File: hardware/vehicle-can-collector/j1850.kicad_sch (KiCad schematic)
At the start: 28 parts, among them Q801 2N7002, Q802 2N7002, Q803 2N7002, Q804 2N7002, Q805 2N7002, Q806 DMG2301L, Q807 2N7002, U801 AS2333Q

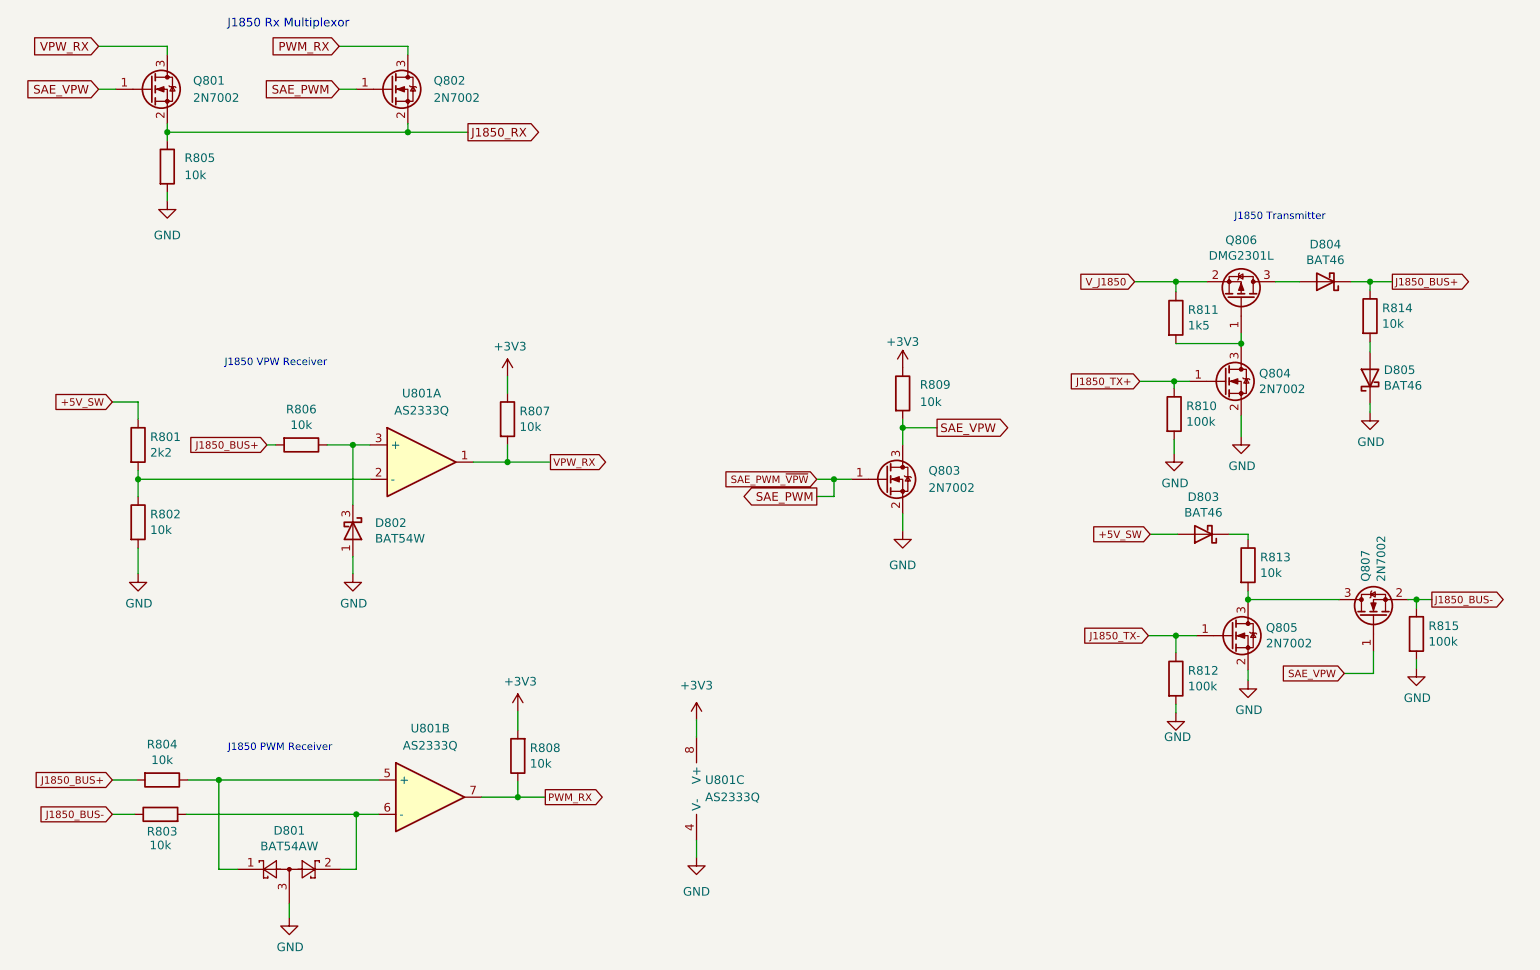
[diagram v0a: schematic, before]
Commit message: Added decoupling, more LEDs, update dts
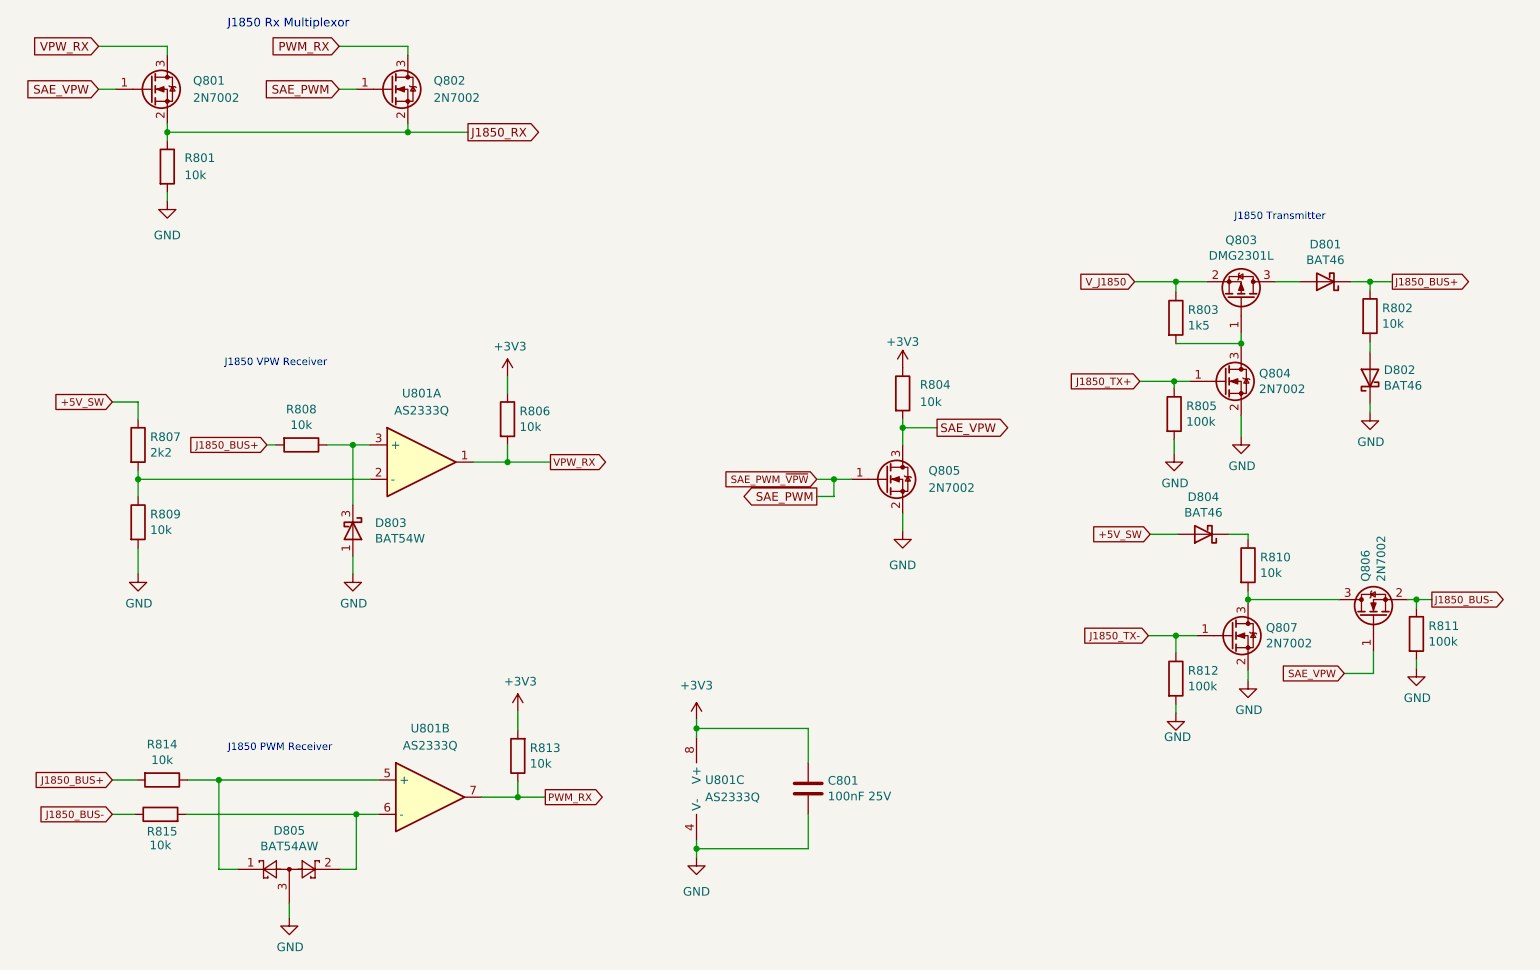
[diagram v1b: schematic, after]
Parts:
- added C801: 100nF 25V, symbol Device:C
- renumbered D804 to D801, D805 to D802, D802 to D803, D803 to D804, D801 to D805, Q806 to Q803, Q803 to Q805, Q807 to Q806, Q805 to Q807, R805 to R801, R814 to R802, R811 to R803, R809 to R804, R810 to R805, R807 to R806, R801 to R807, R806 to R808, R802 to R809, R813 to R810, R815 to R811, R808 to R813, R804 to R814, R803 to R815
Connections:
- net +3V3: now also C801.2
- net GND: now also C801.1
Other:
- company: (none) -> Gavin Hurlbut
- title: (none) -> Vehicle CAN Collector

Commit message: Added footprints, tossed all footprints onto PCB
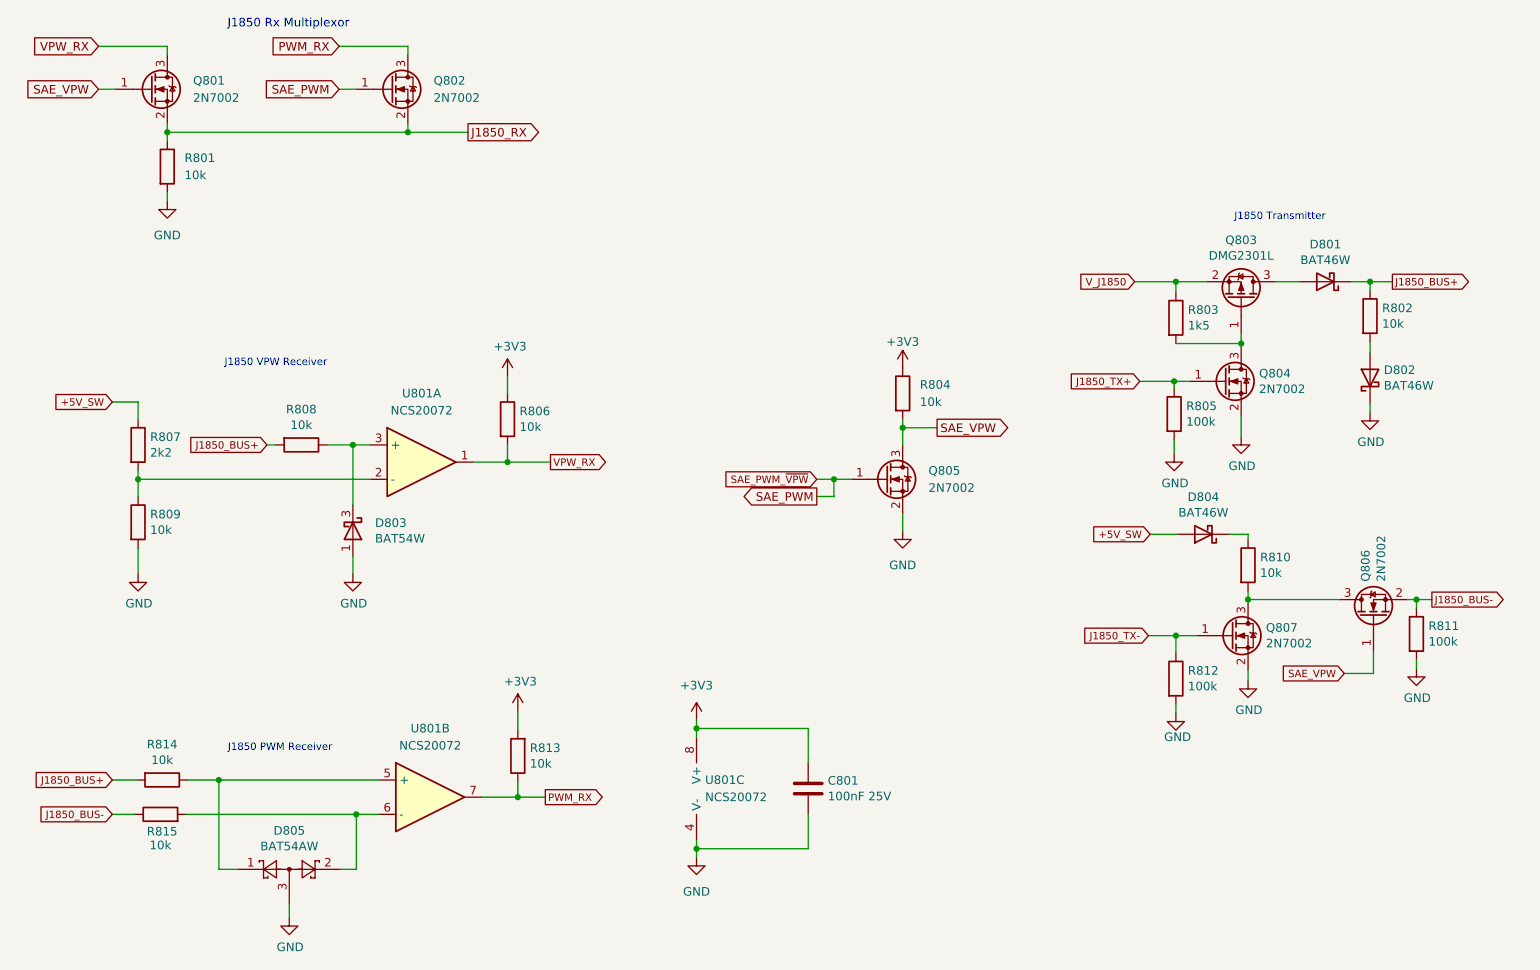
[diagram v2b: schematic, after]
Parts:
- C801: footprint (none) -> Capacitor_SMD:C_0805_2012Metric_Pad1.18x1.45mm_HandSolder
- D801, D802, D804: value BAT46 -> BAT46W; footprint Diode_THT:D_DO-35_SOD27_P7.62mm_Horizontal -> Diode_SMD:D_SOD-123
- R801, R802, R803, R804, R805, R806, R807, R808, R809, R810, R811, R812, R813, R814, R815: footprint (none) -> Resistor_SMD:R_0805_2012Metric_Pad1.20x1.40mm_HandSolder
- U801: value AS2333Q -> NCS20072; footprint Package_SO:SOIC-8_3.9x4.9mm_P1.27mm -> Package_SO:TSSOP-8_4.4x3mm_P0.65mm
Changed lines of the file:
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@@
     (in_bom yes) (on_board yes) (fields_autoplaced)
     (property "Reference" "U801" (id 0) (at 91.44 90.17 0))
-    (property "Value" "AS2333Q" (id 1) (at 91.44 92.71 0))
-    (property "Footprint" "Package_SO:SOIC-8_3.9x4.9mm_P1.27mm" (id 2) (at 91.44 100.33 0)
+    (property "Value" "NCS20072" (id 1) (at 91.44 92.71 0))
+    (property "Footprint" "Package_SO:TSSOP-8_4.4x3mm_P0.65mm" (id 2) (at 91.44 100.33 0)
       (effects (font (size 1.27 1.27)) hide)
     )
@@
     (in_bom yes) (on_board yes)
     (property "Reference" "D804" (id 0) (at 207.01 105.4862 0))
-    (property "Value" "BAT46" (id 1) (at 207.01 107.7976 0))
-    (property "Footprint" "Diode_THT:D_DO-35_SOD27_P7.62mm_Horizontal" (id 2) (at 207.01 106.553 0)
+    (property "Value" "BAT46W" (id 1) (at 207.01 107.7976 0))
+    (property "Footprint" "Diode_SMD:D_SOD-123" (id 2) (at 207.01 106.553 0)
       (effects (font (size 1.27 1.27)) hide)
     )
@@
       (effects (font (size 1.27 1.27)) (justify left))
     )
-    (property "Footprint" "" (id 2) (at 201.168 132.334 90)
+    (property "Footprint" "Resistor_SMD:R_0805_2012Metric_Pad1.20x1.40mm_HandSolder" (id 2) (at 201.168 132.334 90)
       (effects (font (size 1.27 1.27)) hide)
     )
@@
       (effects (font (size 1.27 1.27)) (justify right))
     )
-    (property "Footprint" "" (id 2) (at 107.442 143.764 90)
+    (property "Footprint" "Resistor_SMD:R_0805_2012Metric_Pad1.20x1.40mm_HandSolder" (id 2) (at 107.442 143.764 90)
       (effects (font (size 1.27 1.27)) hide)
     )
@@
     (property "Reference" "R808" (id 0) (at 73.66 92.5322 90))
     (property "Value" "10k" (id 1) (at 73.66 94.8436 90))
-    (property "Footprint" "" (id 2) (at 73.66 96.012 90)
+    (property "Footprint" "Resistor_SMD:R_0805_2012Metric_Pad1.20x1.40mm_HandSolder" (id 2) (at 73.66 96.012 90)
       (effects (font (size 1.27 1.27)) hide)
     )
@@
     (property "Reference" "R815" (id 0) (at 53.086 154.94 90))
     (property "Value" "10k" (id 1) (at 52.832 156.972 90))
-    (property "Footprint" "" (id 2) (at 52.832 154.178 90)
+    (property "Footprint" "Resistor_SMD:R_0805_2012Metric_Pad1.20x1.40mm_HandSolder" (id 2) (at 52.832 154.178 90)
       (effects (font (size 1.27 1.27)) hide)
     )
@@
       (effects (font (size 1.27 1.27)) (justify left))
     )
-    (property "Footprint" "" (id 2) (at 160.782 90.17 90)
+    (property "Footprint" "Resistor_SMD:R_0805_2012Metric_Pad1.20x1.40mm_HandSolder" (id 2) (at 160.782 90.17 90)
       (effects (font (size 1.27 1.27)) hide)
     )
@@
       (effects (font (size 1.27 1.27)) (justify left))
     )
-    (property "Footprint" "" (id 2) (at 52.07 56.642 90)
+    (property "Footprint" "Resistor_SMD:R_0805_2012Metric_Pad1.20x1.40mm_HandSolder" (id 2) (at 52.07 56.642 90)
       (effects (font (size 1.27 1.27)) hide)
     )
@@
       (effects (font (size 1.27 1.27)) (justify left))
     )
-    (property "Footprint" "" (id 2) (at 201.168 78.994 90)
+    (property "Footprint" "Resistor_SMD:R_0805_2012Metric_Pad1.20x1.40mm_HandSolder" (id 2) (at 201.168 78.994 90)
       (effects (font (size 1.27 1.27)) hide)
     )
@@
       (effects (font (size 1.27 1.27)) (justify right))
     )
-    (property "Footprint" "" (id 2) (at 147.6248 144.78 0)
+    (property "Footprint" "Capacitor_SMD:C_0805_2012Metric_Pad1.18x1.45mm_HandSolder" (id 2) (at 147.6248 144.78 0)
       (effects (font (size 1.27 1.27)) hide)
     )
@@
       (effects (font (size 1.27 1.27)) (justify right))
     )
-    (property "Value" "BAT46" (id 1) (at 233.68 89.027 90)
+    (property "Value" "BAT46W" (id 1) (at 233.68 89.027 90)
       (effects (font (size 1.27 1.27)) (justify right))
     )
-    (property "Footprint" "Diode_THT:D_DO-35_SOD27_P7.62mm_Horizontal" (id 2) (at 236.093 87.884 0)
+    (property "Footprint" "Diode_SMD:D_SOD-123" (id 2) (at 236.093 87.884 0)
       (effects (font (size 1.27 1.27)) hide)
     )
@@
       (effects (font (size 1.27 1.27)) (justify left))
     )
-    (property "Footprint" "" (id 2) (at 47.752 109.22 90)
+    (property "Footprint" "Resistor_SMD:R_0805_2012Metric_Pad1.20x1.40mm_HandSolder" (id 2) (at 47.752 109.22 90)
       (effects (font (size 1.27 1.27)) hide)
     )
@@
       (effects (font (size 1.27 1.27)) (justify left))
     )
-    (property "Footprint" "" (id 2) (at 236.728 125.73 90)
+    (property "Footprint" "Resistor_SMD:R_0805_2012Metric_Pad1.20x1.40mm_HandSolder" (id 2) (at 236.728 125.73 90)
       (effects (font (size 1.27 1.27)) hide)
     )
@@
       (effects (font (size 1.27 1.27)) (justify left))
     )
-    (property "Footprint" "" (id 2) (at 47.752 97.79 90)
+    (property "Footprint" "Resistor_SMD:R_0805_2012Metric_Pad1.20x1.40mm_HandSolder" (id 2) (at 47.752 97.79 90)
       (effects (font (size 1.27 1.27)) hide)
     )
@@
     (in_bom yes) (on_board yes) (fields_autoplaced)
     (property "Reference" "U801" (id 0) (at 92.71 139.7 0))
-    (property "Value" "AS2333Q" (id 1) (at 92.71 142.24 0))
-    (property "Footprint" "Package_SO:SOIC-8_3.9x4.9mm_P1.27mm" (id 2) (at 92.71 149.86 0)
+    (property "Value" "NCS20072" (id 1) (at 92.71 142.24 0))
+    (property "Footprint" "Package_SO:TSSOP-8_4.4x3mm_P0.65mm" (id 2) (at 92.71 149.86 0)
       (effects (font (size 1.27 1.27)) hide)
     )
@@
       (effects (font (size 1.27 1.27)) (justify left))
     )
-    (property "Footprint" "" (id 2) (at 211.836 115.57 90)
+    (property "Footprint" "Resistor_SMD:R_0805_2012Metric_Pad1.20x1.40mm_HandSolder" (id 2) (at 211.836 115.57 90)
       (effects (font (size 1.27 1.27)) hide)
     )
@@
     (in_bom yes) (on_board yes)
     (property "Reference" "D801" (id 0) (at 225.044 68.1482 0))
-    (property "Value" "BAT46" (id 1) (at 225.044 70.4596 0))
-    (property "Footprint" "Diode_THT:D_DO-35_SOD27_P7.62mm_Horizontal" (id 2) (at 225.044 69.215 0)
+    (property "Value" "BAT46W" (id 1) (at 225.044 70.4596 0))
+    (property "Footprint" "Diode_SMD:D_SOD-123" (id 2) (at 225.044 69.215 0)
       (effects (font (size 1.27 1.27)) hide)
     )
@@
       (effects (font (size 1.27 1.27)) (justify left))
     )
-    (property "Footprint" "" (id 2) (at 229.87 78.74 90)
+    (property "Footprint" "Resistor_SMD:R_0805_2012Metric_Pad1.20x1.40mm_HandSolder" (id 2) (at 229.87 78.74 90)
       (effects (font (size 1.27 1.27)) hide)
     )
@@
       (effects (font (size 1.27 1.27)) (justify left))
     )
-    (property "Footprint" "" (id 2) (at 200.914 93.218 90)
+    (property "Footprint" "Resistor_SMD:R_0805_2012Metric_Pad1.20x1.40mm_HandSolder" (id 2) (at 200.914 93.218 90)
       (effects (font (size 1.27 1.27)) hide)
     )
@@
       (effects (font (size 1.27 1.27)) (justify left))
     )
-    (property "Footprint" "" (id 2) (at 102.362 93.98 90)
+    (property "Footprint" "Resistor_SMD:R_0805_2012Metric_Pad1.20x1.40mm_HandSolder" (id 2) (at 102.362 93.98 90)
       (effects (font (size 1.27 1.27)) hide)
     )
@@
       (effects (font (size 1.27 1.27)) (justify left))
     )
-    (property "Value" "AS2333Q" (id 1) (at 133.35 149.8599 0)
-      (effects (font (size 1.27 1.27)) (justify left))
-    )
-    (property "Footprint" "Package_SO:SOIC-8_3.9x4.9mm_P1.27mm" (id 2) (at 134.62 148.59 0)
+    (property "Value" "NCS20072" (id 1) (at 133.35 149.8599 0)
+      (effects (font (size 1.27 1.27)) (justify left))
+    )
+    (property "Footprint" "Package_SO:TSSOP-8_4.4x3mm_P0.65mm" (id 2) (at 134.62 148.59 0)
       (effects (font (size 1.27 1.27)) hide)
     )
@@
     (property "Reference" "R814" (id 0) (at 53.086 142.0622 90))
     (property "Value" "10k" (id 1) (at 53.086 144.3736 90))
-    (property "Footprint" "" (id 2) (at 53.086 145.542 90)
-      (effects (font (size 1.27 1.27)) hide)
-    )
+    (property "Footprint" "Resistor_SMD:R_0805_2012Metric_Pad1.20x1.40mm_HandSolder" (id 2) (at 53.086 145.542 90)
+      (effects (font (size 1.27 1.27)) hide)
+    )
